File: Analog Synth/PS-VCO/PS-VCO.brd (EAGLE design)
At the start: 50 x 50 mm, 37 parts, among them IC1 TL084D, Q1 BC847BS, T1 2N3904, T2 2N3904

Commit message: PS-VCO creating PCB
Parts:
- added LED1: (no value), eagle-ltspice:LED_LD260
- added R19: 4.7k, rcl:R0603
- C8, C9: value 10n -> 100n
- moved C7 264.4 mm to (39.0, 46.0), turned to 270 degrees
- moved C8 259.9 mm to (38.5, 35.1)
- moved C4 258.1 mm to (46.2, 46.0), turned to 90 degrees
- moved C9 257.7 mm to (38.5, 28.9), turned to 180 degrees
- moved R18 235.4 mm to (24.0, 34.0), turned to 90 degrees
- moved R15 205.5 mm to (27.0, 18.0), turned to 90 degrees
- moved R17 201.7 mm to (10.0, 7.00)
- moved R16 200.3 mm to (14.0, 10.0), turned to 180 degrees
- moved R14 199.9 mm to (15.4, 19.4), turned to 180 degrees
- moved R4 191.5 mm to (27.0, 21.0), turned to 90 degrees
- moved U$2 188.2 mm to (11.6, 34.8)
- moved R5 187.3 mm to (25.0, 21.0), turned to 90 degrees
- moved C5 187.1 mm to (16.8, 17.2), turned to 180 degrees
- moved C6 184.2 mm to (12.2, 19.0), turned to 270 degrees
- moved SQUARE1 183.0 mm to (7.60, 9.80)
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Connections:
- removed net N$10: CV.P$2, R1.1
- removed net N$13: JP2.1, JP2.2
- removed net N$14: JP2.3, JP2.4
- removed net N$15: JP2.5, JP2.6
- removed net N$17: JP2.7, JP2.8
- removed net N$20: R16.2, R17.2, SQUARE1.P$2
- removed net N$23: JP2.10, JP2.9
- new net CV_IN: CV.P$2, JP2.10, JP2.9, R1.1
- new net CV_LED: IC1.6, IC1.7, R6.1
- new net SQUARE_OUT: JP2.7, JP2.8, R16.2, R17.2, SQUARE1.P$2
- net +12V: now also JP2.1, JP2.2
- net -12V: now also C7.-, C9.2, JP2.5, JP2.6; no longer C7.+, C9.1
- net GND: now also C7.+, C9.1, JP2.3, JP2.4, R19.2; no longer C7.-, C9.2
- net N$11: now also IC1.5; no longer IC1.3
- net N$12: now also LED1.K, R19.1; no longer IC1.1, IC1.2, R6.1
- net N$18: now also LED1.A
- net N$21: now also IC1.1; no longer IC1.7
- net N$22: now also IC1.2; no longer IC1.6
- net N$6: now also IC1.3; no longer IC1.5
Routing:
- net GND: track 0.00 -> 209.6 mm, vias 0 -> 3
- net CV_IN: track 0.00 -> 103.8 mm
- net +12V: track 0.00 -> 99.6 mm, vias 0 -> 4
- net -12V: track 0.00 -> 81.3 mm, vias 0 -> 2
- net CURRENT_SINK: track 0.00 -> 53.4 mm, vias 0 -> 3
- net SQUARE_OUT: track 0.00 -> 47.9 mm
- net N$22: track 0.00 -> 25.0 mm
- net N$18: track 0.00 -> 22.8 mm, vias 0 -> 2
- net N$4: track 0.00 -> 20.2 mm
- net N$19: track 0.00 -> 19.2 mm, vias 0 -> 1
- net N$3: track 0.00 -> 17.0 mm, vias 0 -> 2
- net N$16: track 0.00 -> 16.5 mm, vias 0 -> 2
- net N$1: track 0.00 -> 16.3 mm, vias 0 -> 2
- net N$9: track 0.00 -> 15.7 mm
- net N$6: track 0.00 -> 14.4 mm, vias 0 -> 2
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
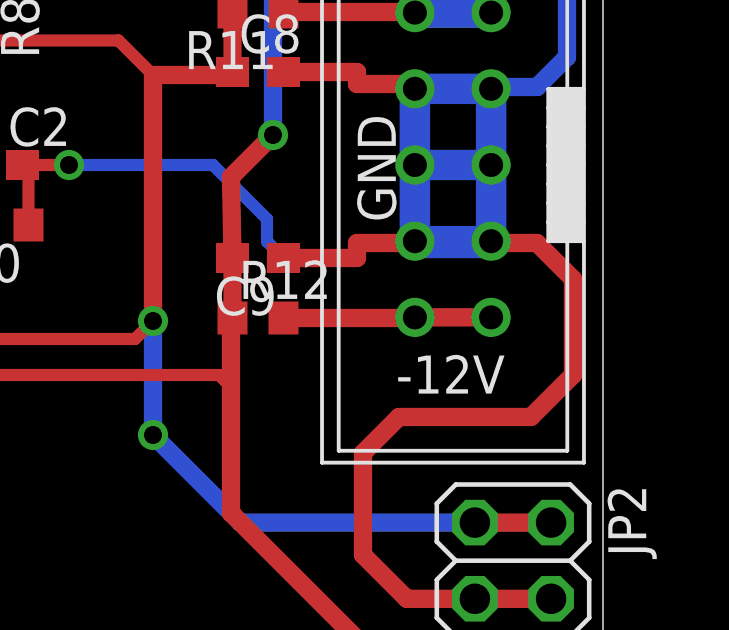
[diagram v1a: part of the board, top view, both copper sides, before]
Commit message: PS-VCO still working on PCB - making gerbers. proof reading. Need to add an LED for the CV signal
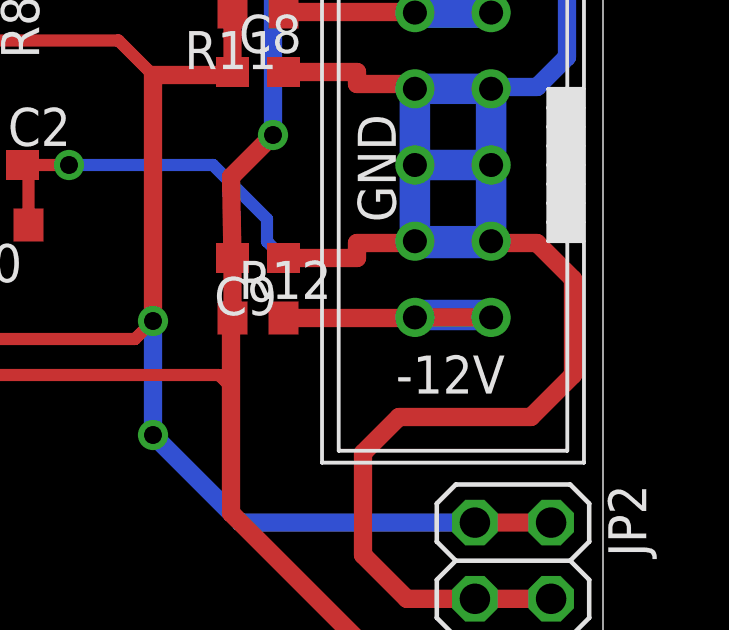
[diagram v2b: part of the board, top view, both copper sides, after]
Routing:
- net N$10: track 0.00 -> 2.20 mm
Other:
- board text added: "+12"
- board text added: "-12"
- board text added: "2015"
- board text added: "CV_IN"
- board text added: "GND"
- board text added: "PS-VCO"
- board text added: "Ryan Jensen"
- board text added: "SQUARE"
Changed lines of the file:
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@@
 <dimension x1="0" y1="0" x2="50" y2="0" x3="25" y3="-14" textsize="1.778" layer="19"/>
 <dimension x1="0" y1="0" x2="0" y2="50" x3="-13" y3="25" textsize="1.778" layer="19"/>
+<text x="42" y="19.6" size="0.8128" layer="27">+12</text>
+<text x="42" y="17.2" size="0.8128" layer="27">GND</text>
+<text x="42" y="14.6" size="0.8128" layer="27">-12</text>
+<text x="40.8" y="12.2" size="0.8128" layer="27">CV_IN</text>
+<text x="39.8" y="9.6" size="0.8128" layer="27">SQUARE</text>
+<text x="15.2" y="0.6" size="6.4516" layer="27">PS-VCO</text>
+<text x="15.4" y="7.6" size="1.27" layer="27">Ryan Jensen</text>
+<text x="27" y="0.4" size="1.27" layer="27">2015</text>
 </plain>
 <attributes>
@@
 <wire x1="9.63" y1="13.9" x2="9.73" y2="14" width="0.4064" layer="1"/>
 </signal>
+<signal name="N$10">
+<wire x1="46" y1="27" x2="43.8" y2="27" width="1.016" layer="16"/>
+</signal>
 </signals>

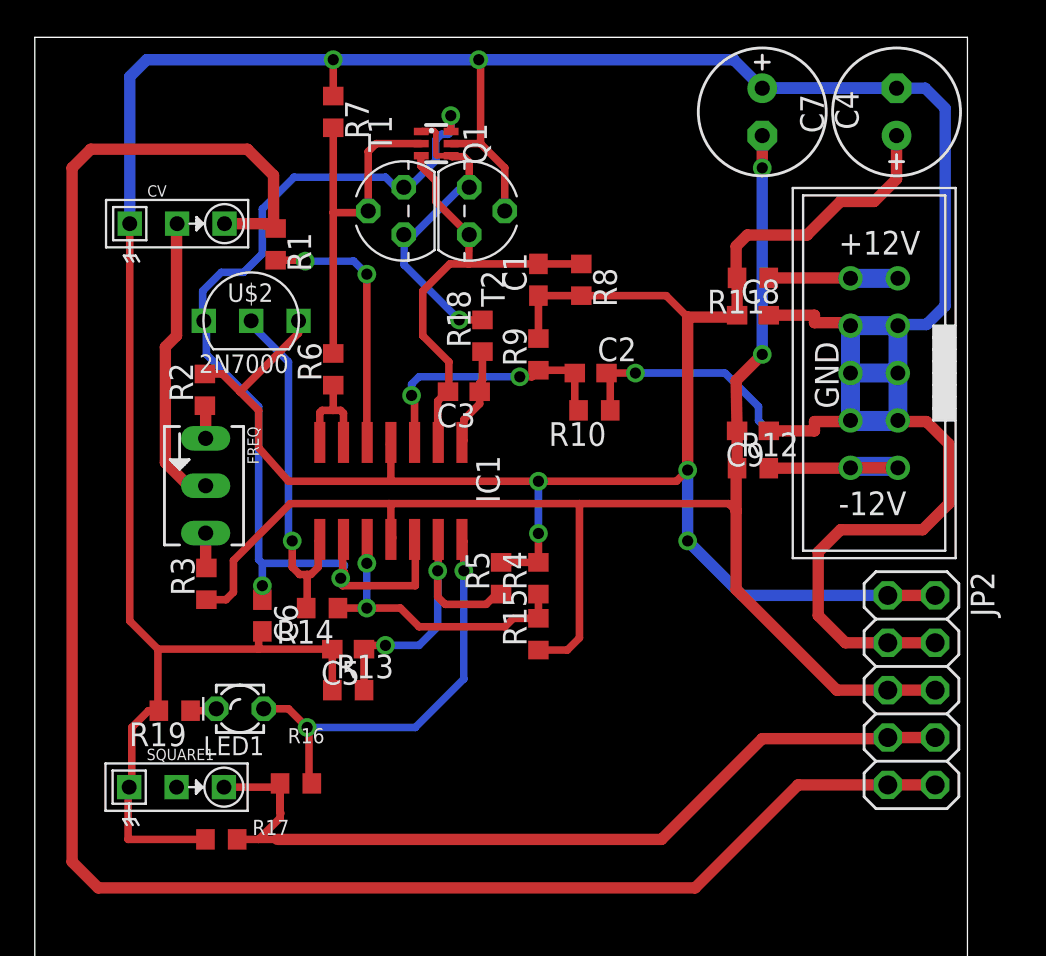
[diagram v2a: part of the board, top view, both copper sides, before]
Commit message: PS-VCO added LED - organizing text on PCB
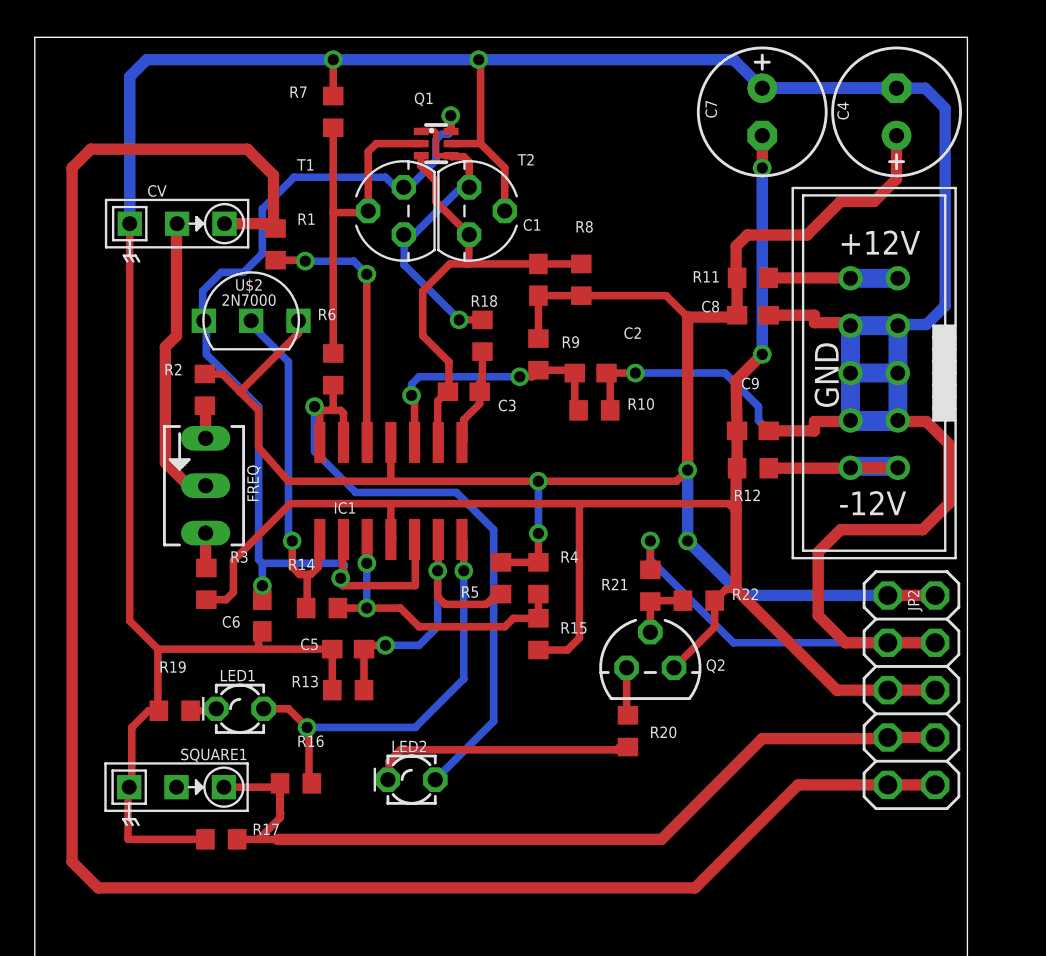
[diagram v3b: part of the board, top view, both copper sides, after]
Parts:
- added LED2: (no value), eagle-ltspice:LED_LD260
- added Q2: 2N3906, transistor-pnp:TO92
- added R20: 3.3k, rcl:R0603
- added R21: 47k, rcl:R0603
- added R22: 33k, rcl:R0603
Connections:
- new net N$13: Q2.3, R20.2
- new net N$14: LED2.K, R20.1
- new net N$15: Q2.2, R21.2, R22.1
- net -12V: now also Q2.1, R22.2
- net CV_LED: now also LED2.A
- net GND: now also R21.1
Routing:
- net CV_LED: track 5.90 -> 34.8 mm, vias 0 -> 1
- net GND: track 209.6 -> 226.7 mm, vias 3 -> 4
- net N$14: track 0.00 -> 14.1 mm
- net -12V: track 81.3 -> 87.2 mm
- net N$15: track 0.00 -> 3.42 mm
- net N$13: track 0.00 -> 2.58 mm

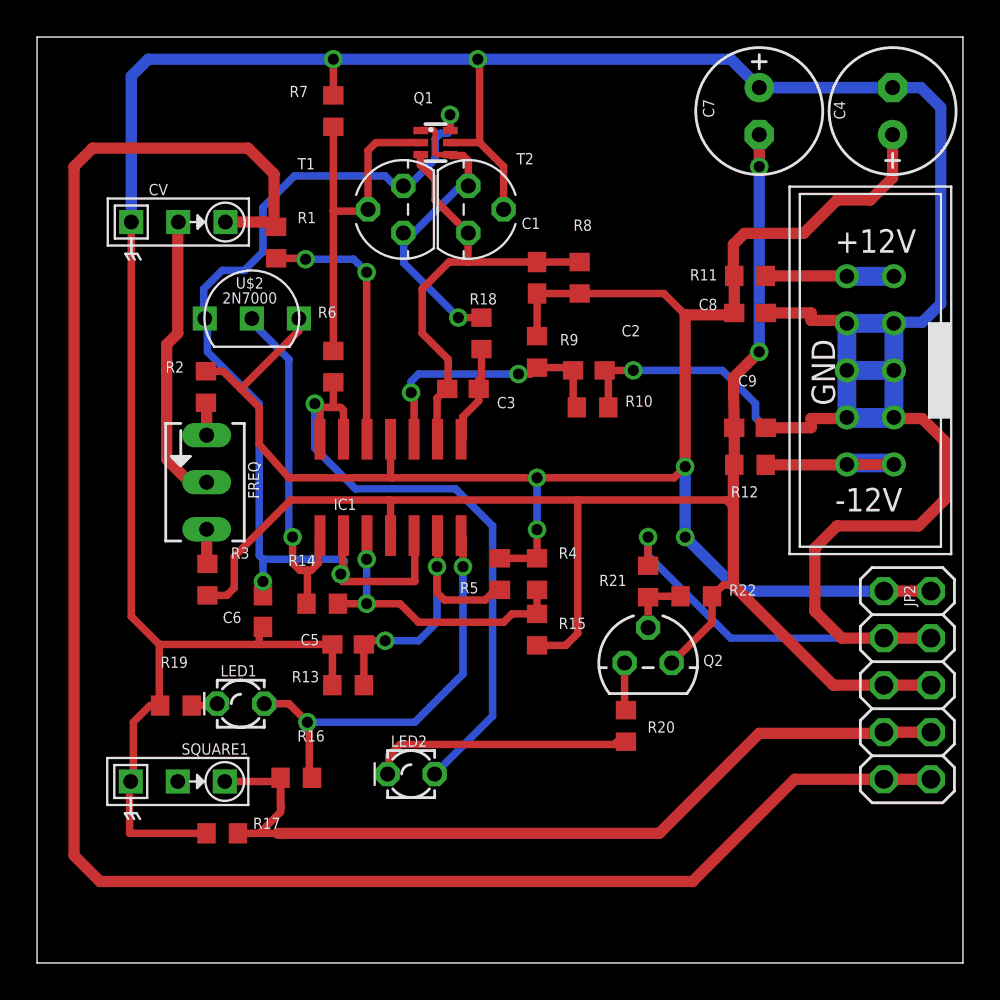
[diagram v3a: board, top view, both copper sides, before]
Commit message: PS-VCO updating schematic. made it look cleaner. Added information about theory of operation and instructions for building.
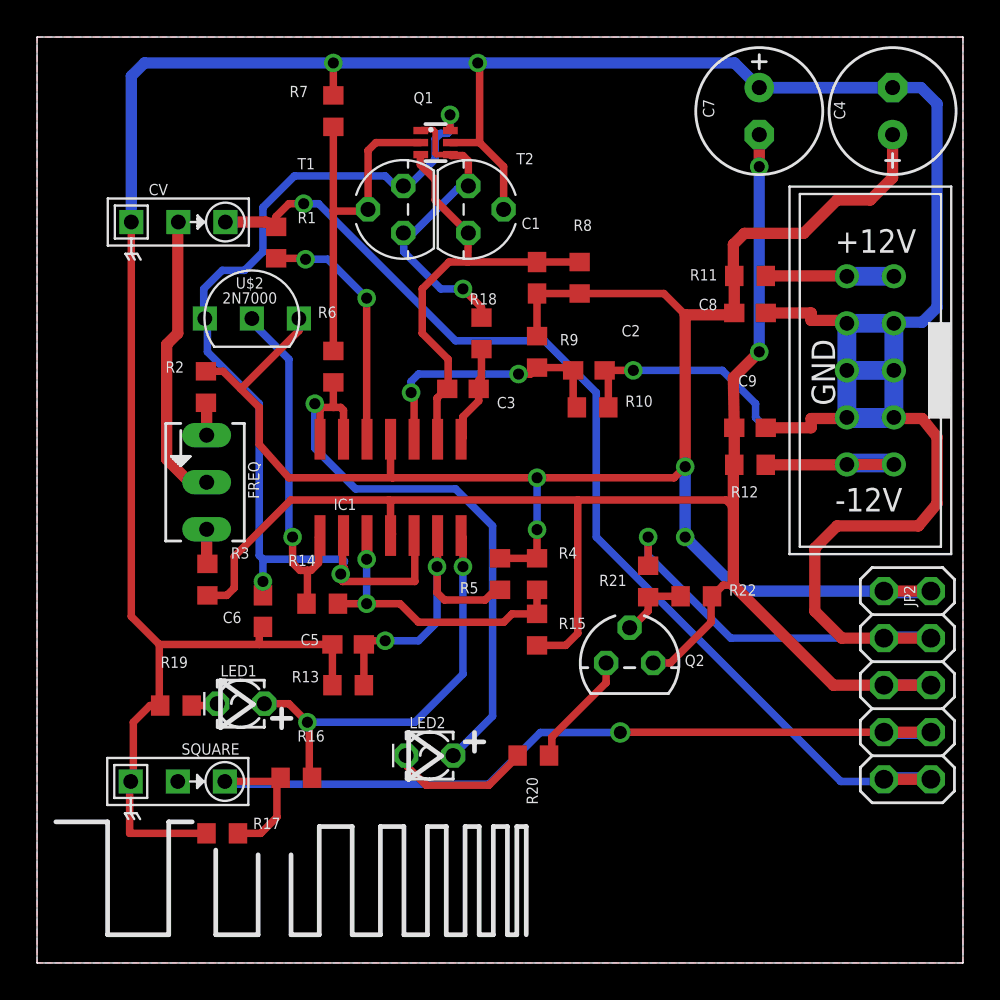
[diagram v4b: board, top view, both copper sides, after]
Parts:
- moved R20 5.25 mm to (26.8, 11.2), turned to 0 degrees
- moved LED2 1.41 mm to (21.2, 11.2)
- moved Q2 1.00 mm to (32.0, 16.2)
- renumbered SQUARE1 to SQUARE
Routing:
- net CV_IN: track 103.8 -> 56.5 mm, vias 0 -> 1
- net N$14: track 14.1 -> 7.69 mm
- net N$13: track 2.58 -> 6.28 mm
- net N$25: track 0.00 -> 2.40 mm
- net N$24: track 0.00 -> 2.40 mm
- net N$23: track 0.00 -> 2.40 mm
- net N$20: track 0.00 -> 2.40 mm
- net N$17: track 0.00 -> 2.00 mm
- net CV_LED: track 34.8 -> 33.4 mm
- net GND: track 226.7 -> 225.8 mm
- net -12V: track 87.2 -> 88.2 mm
- net N$11: track 14.2 -> 13.4 mm
- net SQUARE_OUT: track 47.9 -> 47.4 mm, vias 0 -> 1
- net N$3: track 17.0 -> 16.9 mm, vias 2 -> 1
- added copper zone on layer 1, net GND
- added copper zone on layer 16, net GND
